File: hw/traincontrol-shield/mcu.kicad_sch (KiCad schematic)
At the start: 7 parts, among them J1 ESP32-S3 Header L, J2 ESP32-S3 Header R

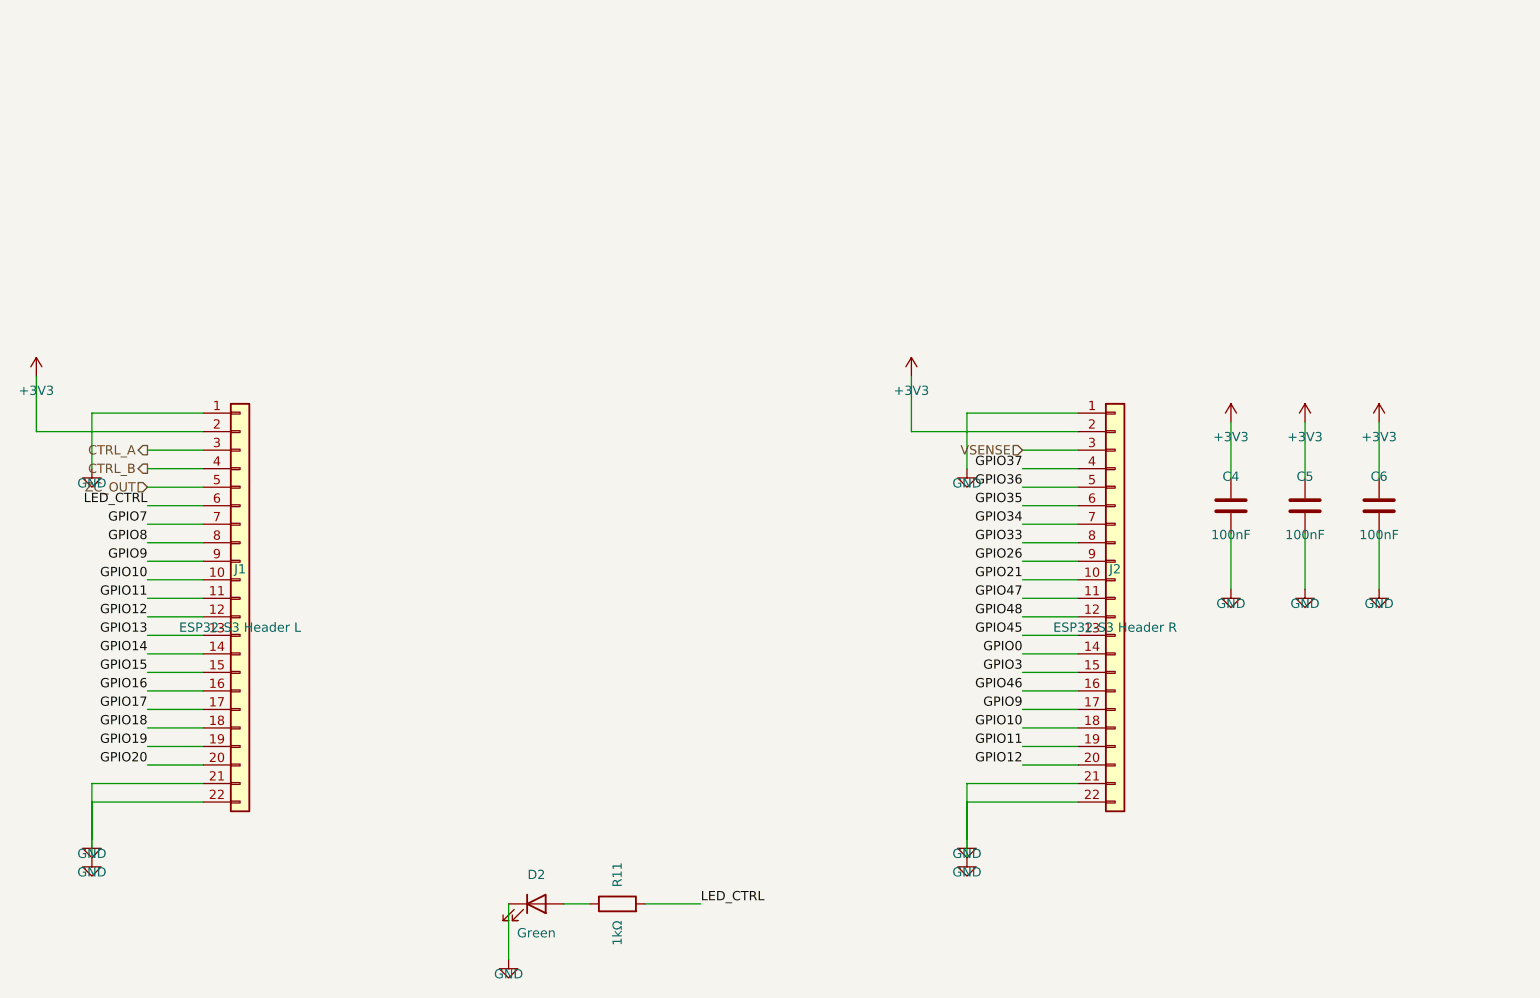
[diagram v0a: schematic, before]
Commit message: Schematic updates by hand.
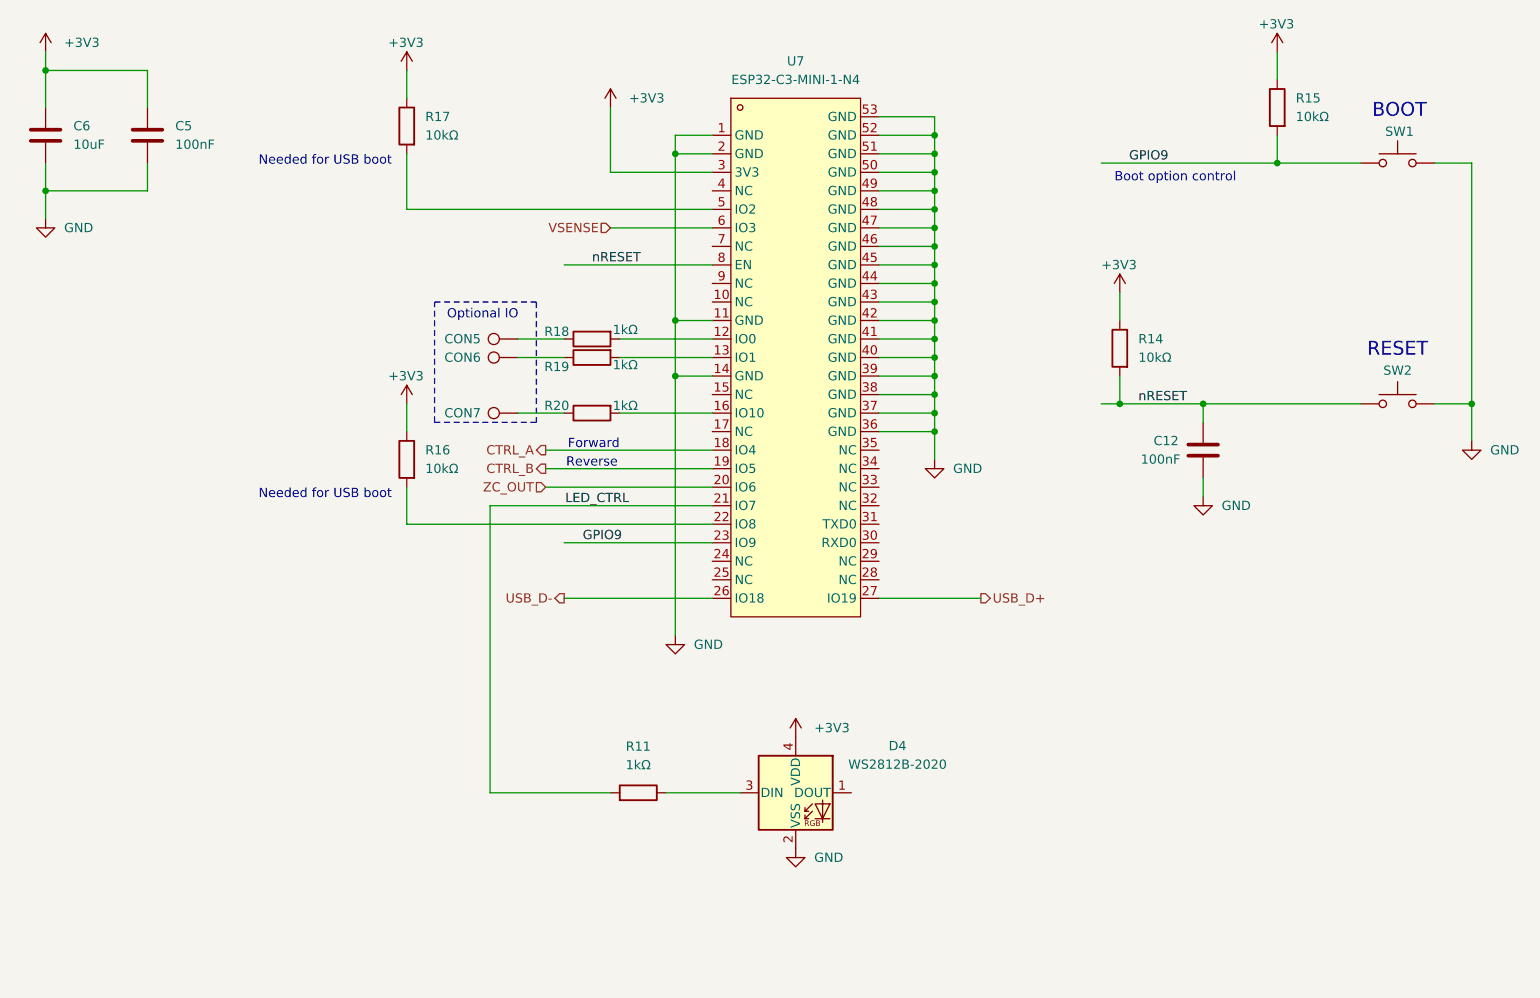
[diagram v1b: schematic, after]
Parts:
- removed C4: 100nF, Capacitor_SMD:C_0603_1608Metric, symbol Device:C
- removed D2: Green, LED_SMD:LED_0603_1608Metric, symbol Device:LED
- removed J1: ESP32-S3 Header L, Connector_PinHeader_2.54mm:PinHeader_1x22_P2.54mm_Vertical, symbol Connector_Generic:Conn_01x22
- removed J2: ESP32-S3 Header R, Connector_PinHeader_2.54mm:PinHeader_1x22_P2.54mm_Vertical, symbol Connector_Generic:Conn_01x22
- added C12: 100nF, Capacitor_SMD:C_0603_1608Metric, symbol Device:C
- added CON5, CON6, CON7: ConnectionPad, TestPoint:TestPoint_Pad_D2.0mm, symbol Connector:TestPoint
- added D4: WS2812B-2020, LED_SMD:LED_WS2812B-2020_PLCC4_2.0x2.0mm, symbol LED:WS2812B-2020
- added R14, R15, R16, R17: 10kΩ, Resistor_SMD:R_0603_1608Metric, symbol Device:R
- added R18, R19, R20: 1kΩ, Resistor_SMD:R_0603_1608Metric, symbol Device:R
- added SW1, SW2: SW_Push, Button_Switch_SMD:SW_SPST_TL3342, symbol Switch:SW_Push
- added U7: ESP32-C3-MINI-1-N4, traincontrol-shield:WIFIM-SMD_ESP32-C3-MINI-1, symbol traincontrol-shield:ESP32-C3-MINI-1-N4
- C6: value 100nF -> 10uF
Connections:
- net +3V3: now also D4.4 (VDD), R14.1, R15.1, R16.1, R17.1, U7.3 (3V3)
- net CTRL_A: now also U7.18 (IO4)
- net CTRL_B: now also U7.19 (IO5)
- net GND: now also C12.2, D4.2 (VSS), SW1.2, SW2.2, U7.1 (GND), U7.11 (GND), U7.14 (GND), U7.2 (GND), U7.36 (GND), U7.37 (GND), U7.38 (GND), U7.39 (GND), U7.40 (GND), U7.41 (GND), U7.42 (GND), U7.43 (GND), U7.44 (GND), U7.45 (GND), U7.46 (GND), U7.47 (GND), U7.48 (GND), U7.49 (GND), U7.50 (GND), U7.51 (GND), U7.52 (GND), U7.53 (GND)
- net GPIO9: now also R15.2, SW1.1, U7.23 (IO9)
- net LED_CTRL: now also U7.21 (IO7)
- net VSENSE: now also U7.6 (IO3)
- net ZC_OUT: now also U7.20 (IO6)
- net at R11.1: now also D4.3 (DIN)
- new net: R17.2, U7.5 (IO2)
- new net: CON7.1, R20.1
- new net: R20.2, U7.16 (IO10)
- new net: R18.2, U7.12 (IO0)
- new net: R19.2, U7.13 (IO1)
- new net: R16.2, U7.22 (IO8)
- new net: CON6.1, R19.1
- new net: CON5.1, R18.1
- new net USB_D+: U7.27 (IO19)
- new net USB_D-: U7.26 (IO18)
- new net nRESET: C12.1, R14.2, SW2.1, U7.8 (EN)
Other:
- note added: "BOOT"
- note added: "Boot option control"
- note added: "Forward"
- note added: "Needed for USB boot"
- note added: "Optional IO"
- note added: "RESET"
- note added: "Reverse"
- moved on the sheet: C6, R11
